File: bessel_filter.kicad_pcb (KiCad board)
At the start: 2 copper layers, 30 x 35 mm, 9 parts, among them J1 Conn_Coaxial, J2 Conn_Coaxial

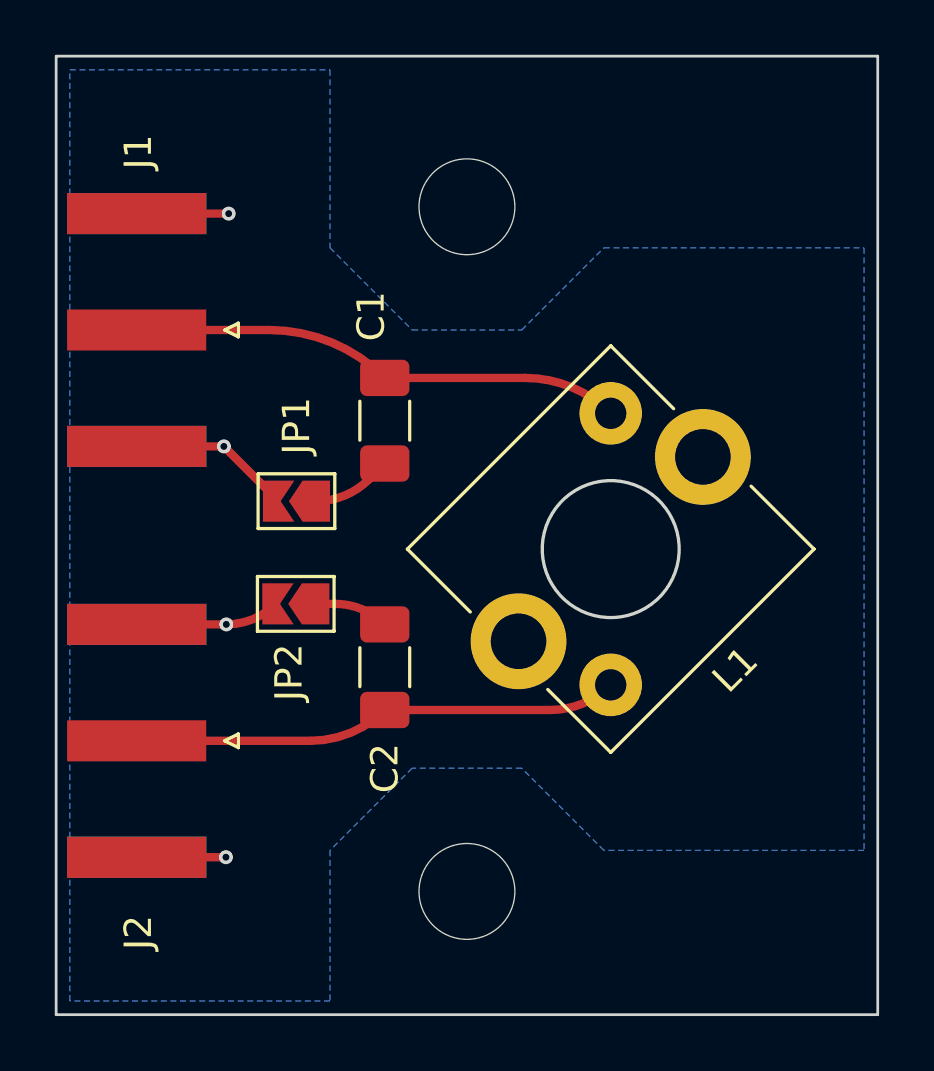
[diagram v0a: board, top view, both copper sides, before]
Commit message: Finished layout for 3rd order-fixed L
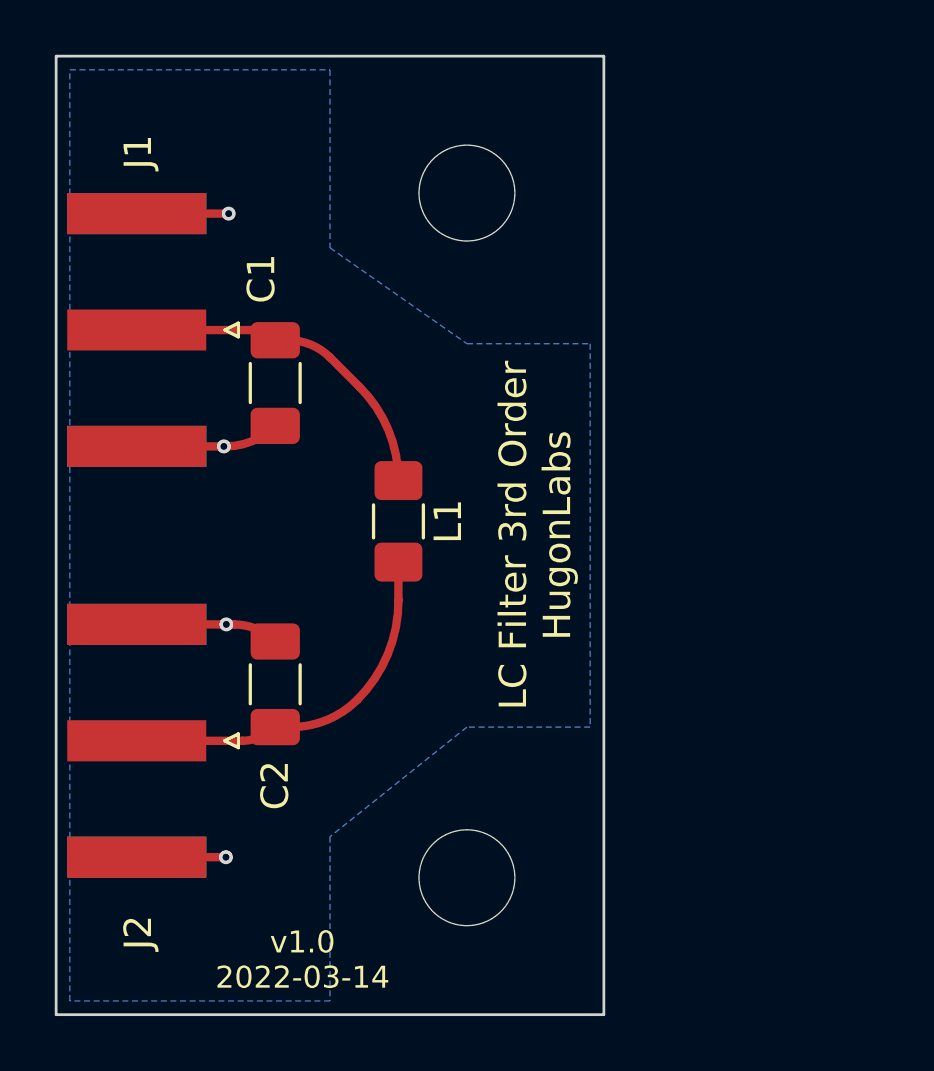
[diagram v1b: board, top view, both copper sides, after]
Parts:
- removed JP1, JP2: SolderJumper_2_Bridged, Jumper:SolderJumper-2_P1.3mm_Open_TrianglePad1.0x1.5mm
- L1: value L_Trim -> L; footprint HugonLib:Coil_Craft_Unicoil_10mm_gnd_shield -> Inductor_SMD:L_1206_3216Metric_Pad1.42x1.75mm_HandSolder
- moved L1 7.82 mm to (125.0, 82.0), turned to -90 degrees
- moved C1 4.23 mm to (120.5, 76.9)
- moved C2 4.05 mm to (120.5, 87.9)
- moved REF** 0.50 mm to (127.5, 70.0)
- moved REF** 0.50 mm to (127.5, 95.0)
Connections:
- C1 pad 2: Net-(C1-Pad2) -> /GND
- C2 pad 2: Net-(C2-Pad2) -> /GND
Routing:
- net /sig_in: track 18.1 -> 12.6 mm
- net /sig_out: track 17.8 -> 13.8 mm
- net Net-(C1-Pad2): track 2.94 -> 0.00 mm
- net Net-(C2-Pad2): track 2.71 -> 0.00 mm
- net /GND: track 17.9 -> 17.1 mm
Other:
- board size 30 x 35 mm -> 20 x 35 mm
- board text added: "20.1000 mm x 35.1000 mm"
- board text added: "LC Filter 3rd Order HugonLabs"
- board text added: "LC Filter 3rd Order v1.0 2022-03-14 HugonLabs"
- board text added: "v1.0 2022-03-14"
- board text removed: "30.1000 mm x 35.1000 mm"
- board text removed: "3rd Order LC Filter-Trim v1.0 2022-03-13 HugonLabs"
